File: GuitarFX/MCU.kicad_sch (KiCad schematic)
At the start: 42 parts, among them J301 USB_C_Receptacle_USB2.0, J302 Conn_ARM_SWD_TagConnect_TC2030, J303 Screw_Terminal_01x06, U2 STM32H733VGTx, U301 USBLC6-2SC6, Y301 24MHz

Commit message: Created RGB LED footprint
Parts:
- D303: footprint (none) -> Custom_Footprints_KiCAD7:LED_SMD_RGB_AAA3528LSEEZGKQBKS
- FL301: footprint ACM20129002PTL002 -> (none)

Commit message: Assigned all footprints
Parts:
- added SW301: SW_SPDT, Button_Switch_SMD:SW_SPDT_PCM12, symbol Switch:SW_SPDT
- FB301, FB302: footprint (none) -> Inductor_SMD:L_0603_1608Metric
- FL301: footprint (none) -> ACM2012-900-2P-TL002:ACM20129002PTL002
- J301: footprint (none) -> Connector_USB:USB_C_Receptacle_Molex_105450-0101
- J303: footprint (none) -> TerminalBlock_Phoenix:TerminalBlock_Phoenix_MPT-0,5-6-2.54_1x06_P2.54mm_Horizontal
- R301, R303, R304: footprint (none) -> Resistor_SMD:R_0402_1005Metric
- R302, R305, R306, R307, R308: footprint (none) -> Resistor_SMD:R_0603_1608Metric
- R309, R310: value 1k -> 325R; footprint (none) -> Resistor_SMD:R_0603_1608Metric
- R311: value 1k -> 750R; footprint (none) -> Resistor_SMD:R_0603_1608Metric
- Y301: footprint (none) -> Crystal:Crystal_SMD_3225-4Pin_3.2x2.5mm
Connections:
- net +3.3V: now also SW301.3 (C)
- net GND: now also SW301.1 (A); no longer R301.1
- new net: R301.1, SW301.2 (B)
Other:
- note removed: "Figure out resistor values when selecting RGB LED"
- moved on the sheet: R301

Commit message: Updated USBC connector part and confirmed it is on JLC
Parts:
- J301: footprint Connector_USB:USB_C_Receptacle_Molex_105450-0101 -> Connector_USB:USB_C_Receptacle_HRO_TYPE-C-31-M-12

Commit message: Finished rough layout for MCU
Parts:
- C302: footprint Capacitor_SMD:C_0603_1608Metric -> Capacitor_SMD:C_0402_1005Metric

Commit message: Finished rough layout
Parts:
- removed D2: SMAJ15A, Diode_SMD:D_SMA, symbol Diode:SMAJ15A
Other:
- moved on the sheet: C311, C312, FB302

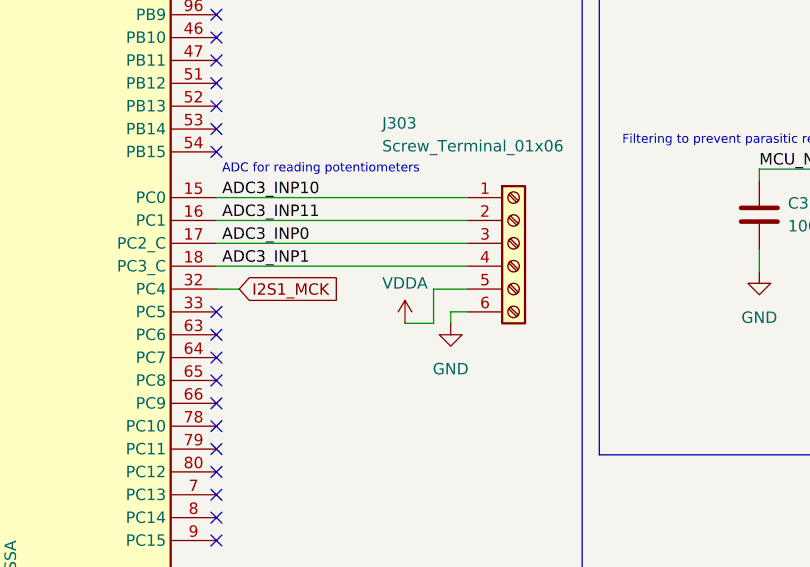
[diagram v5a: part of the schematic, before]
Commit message: Made position changes to nicer coordinates, and added edge cuts
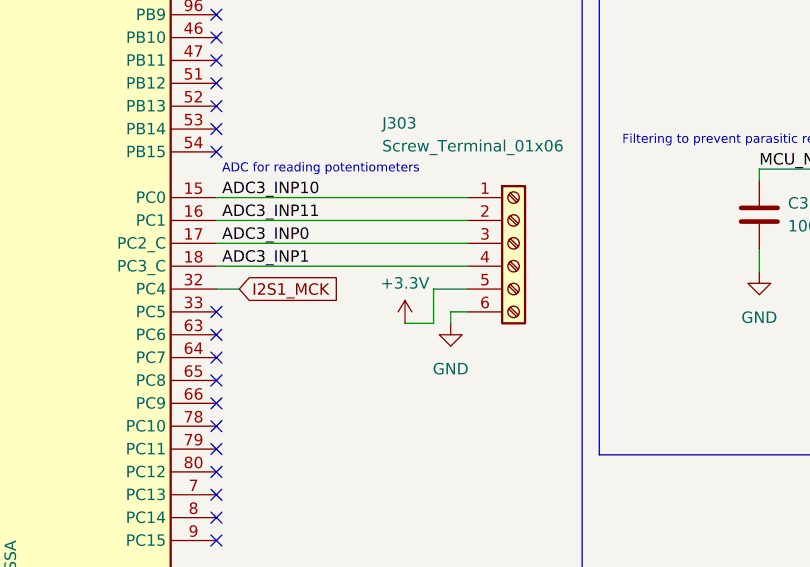
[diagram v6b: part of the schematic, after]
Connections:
- net +3.3V: now also J303.5 (Pin_5)
- net VDDA: no longer J303.5 (Pin_5)

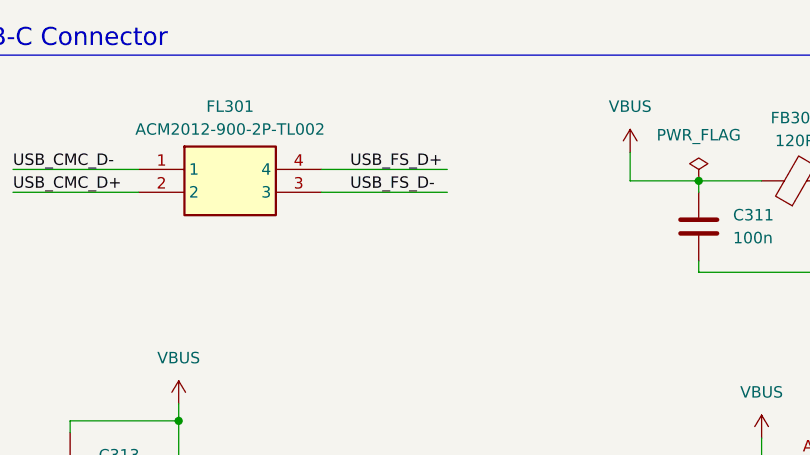
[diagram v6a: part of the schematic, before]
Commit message: USB routing complete
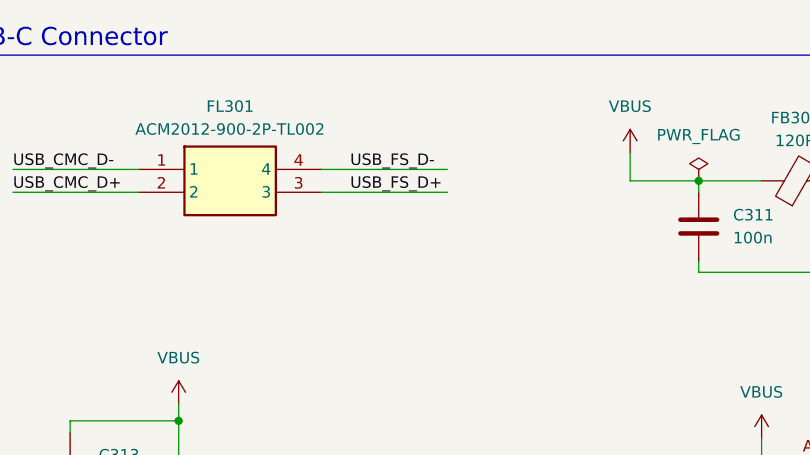
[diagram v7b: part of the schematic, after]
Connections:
- net USB_FS_D+: now also FL301.3; no longer FL301.4
- net USB_FS_D-: now also FL301.4; no longer FL301.3

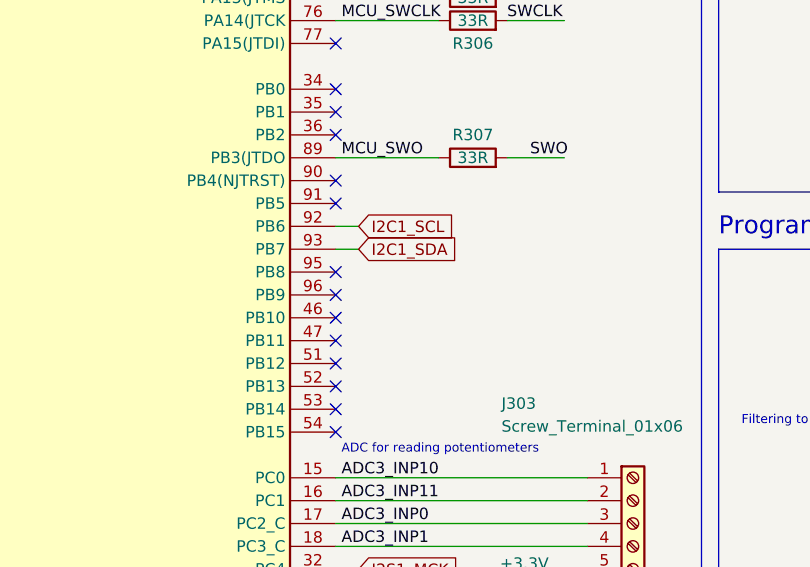
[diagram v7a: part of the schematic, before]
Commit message: Updated I2C pins for easier routing
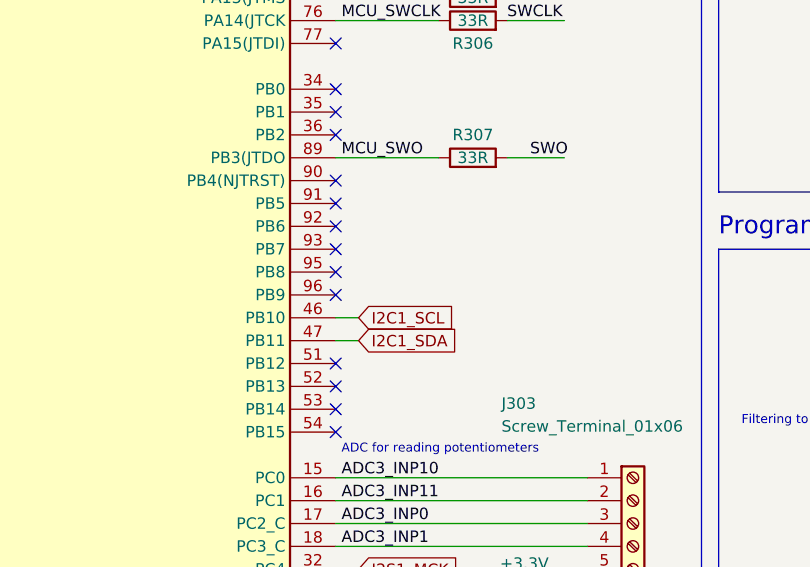
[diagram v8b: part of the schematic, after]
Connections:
- net I2C1_SCL: now also U2.46 (PB10); no longer U2.92 (PB6)
- net I2C1_SDA: now also U2.47 (PB11); no longer U2.93 (PB7)
